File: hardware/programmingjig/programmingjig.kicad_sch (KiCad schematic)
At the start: 15 parts, among them J1 SPGM, J11 PGMIO, J2 USB_C_Receptacle_USB2.0, J3 PGMVDD, J4 PGMO, J5 PGMVDD-POGO-5.5mm, U2 RS3236-3.3YUTDN4, U3 CH32V003JxMx

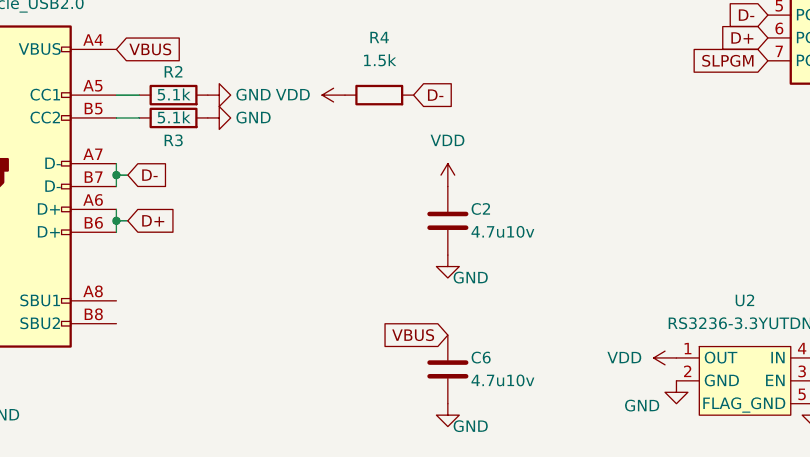
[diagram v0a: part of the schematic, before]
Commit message: Add firmware for programming jig
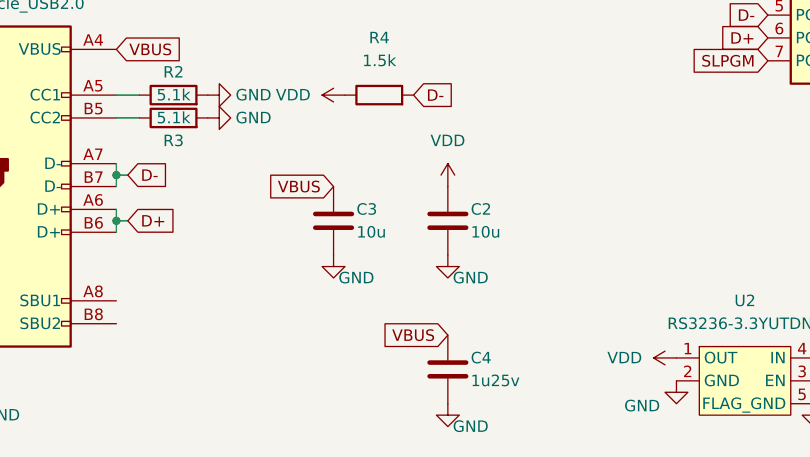
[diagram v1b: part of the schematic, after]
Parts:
- removed C6: 4.7u10v, Capacitor_SMD:C_0402_1005Metric, symbol Device:C
- added C3: 10u, Capacitor_SMD:C_0603_1608Metric, symbol Device:C
- added C4: 1u25v, Capacitor_SMD:C_0402_1005Metric, symbol Device:C
- C2: value 4.7u10v -> 10u; footprint Capacitor_SMD:C_0402_1005Metric -> Capacitor_SMD:C_0603_1608Metric; LCSC C23733 -> C19702
- J11, J3, J5: LCSC C5221281 -> C5221294
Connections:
- net GND: now also C3.2, C4.2
- net VBUS: now also C3.1, C4.1
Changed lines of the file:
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@@
+	(global_label "VBUS"
+		(shape input)
+		(at 101.6 60.96 180)
+		(fields_autoplaced yes)
+		(effects
+			(font
+				(size 1.27 1.27)
+			)
+			(justify right)
+		)
+		(property "Intersheetrefs" "${INTERSHEET_REFS}"
+			(at 94.2883 61.0394 0)
+			(effects
+				(font
+					(size 1.27 1.27)
+				)
+				(justify right)
+				(hide yes)
+			)
+		)
+	)
 	(global_label "VBUS"
 		(shape input)
@@
 			)
 		)
-		(property "LCSC" "C5221281"
+		(property "LCSC" "C5221294"
 			(at 218.44 60.96 0)
 			(effects
@@
 				(path "/fb00fef0-158e-4651-97d6-849960de9d61"
 					(reference "#PWR18")
+					(unit 1)
+				)
+			)
+		)
+	)
+	(symbol
+		(lib_id "power:GND")
+		(at 101.6 68.58 0)
+		(unit 1)
+		(exclude_from_sim no)
+		(in_bom yes)
+		(on_board yes)
+		(dnp no)
+		(property "Reference" "#PWR22"
+			(at 101.6 74.93 0)
+			(effects
+				(font
+					(size 1.27 1.27)
+				)
+				(hide yes)
+			)
+		)
+		(property "Value" "GND"
+			(at 104.14 71.12 0)
+			(effects
+				(font
+					(size 1.27 1.27)
+				)
+			)
+		)
+		(property "Footprint" ""
+			(at 101.6 68.58 0)
+			(effects
+				(font
+					(size 1.27 1.27)
+				)
+				(hide yes)
+			)
+		)
+		(property "Datasheet" ""
+			(at 101.6 68.58 0)
+			(effects
+				(font
+					(size 1.27 1.27)
+				)
+				(hide yes)
+			)
+		)
+		(property "Description" ""
+			(at 101.6 68.58 0)
+			(effects
+				(font
+					(size 1.27 1.27)
+				)
+				(hide yes)
+			)
+		)
+		(pin "1"
+		)
+		(instances
+			(project "programmingjig"
+				(path "/fb00fef0-158e-4651-97d6-849960de9d61"
+					(reference "#PWR22")
 					(unit 1)
 				)
@@
 	)
 	(symbol
+		(lib_id "Device:C")
+		(at 101.6 64.77 0)
+		(unit 1)
+		(exclude_from_sim no)
+		(in_bom yes)
+		(on_board yes)
+		(dnp no)
+		(property "Reference" "C3"
+			(at 104.14 63.5 0)
+			(effects
+				(font
+					(size 1.27 1.27)
+				)
+				(justify left)
+			)
+		)
+		(property "Value" "10u"
+			(at 104.14 66.04 0)
+			(effects
+				(font
+					(size 1.27 1.27)
+				)
+				(justify left)
+			)
+		)
+		(property "Footprint" "Capacitor_SMD:C_0603_1608Metric"
+			(at 102.5652 68.58 0)
+			(effects
+				(font
+					(size 1.27 1.27)
+				)
+				(hide yes)
+			)
+		)
+		(property "Datasheet" ""
+			(at 101.6 64.77 0)
+			(effects
+				(font
+					(size 1.27 1.27)
+				)
+				(hide yes)
+			)
+		)
+		(property "Description" ""
+			(at 101.6 64.77 0)
+			(effects
+				(font
+					(size 1.27 1.27)
+				)
+				(hide yes)
+			)
+		)
+		(property "LCSC" "C19702"
+			(at 101.6 64.77 0)
+			(effects
+				(font
+					(size 1.27 1.27)
+				)
+				(hide yes)
+			)
+		)
+		(pin "1"
+		)
+		(pin "2"
+		)
+		(instances
+			(project "programmingjig"
+				(path "/fb00fef0-158e-4651-97d6-849960de9d61"
+					(reference "C3")
+					(unit 1)
+				)
+			)
+		)
+	)
+	(symbol
 		(lib_id "Device:R")
 		(at 83.82 50.8 90)
@@
 			)
 		)
-		(property "LCSC" "C5221281"
+		(property "LCSC" "C5221294"
 			(at 218.44 68.58 0)
 			(effects
@@
 				(path "/fb00fef0-158e-4651-97d6-849960de9d61"
 					(reference "C1")
-					(unit 1)
-				)
-			)
-		)
-	)
-	(symbol
-		(lib_id "Device:C")
-		(at 114.3 81.28 0)
-		(unit 1)
-		(exclude_from_sim no)
-		(in_bom yes)
-		(on_board yes)
-		(dnp no)
-		(property "Reference" "C6"
-			(at 116.84 80.01 0)
-			(effects
-				(font
-					(size 1.27 1.27)
-				)
-				(justify left)
-			)
-		)
-		(property "Value" "4.7u10v"
-			(at 116.84 82.55 0)
-			(effects
-				(font
-					(size 1.27 1.27)
-				)
-				(justify left)
-			)
-		)
-		(property "Footprint" "Capacitor_SMD:C_0402_1005Metric"
-			(at 115.2652 85.09 0)
-			(effects
-				(font
-					(size 1.27 1.27)
-				)
-				(hide yes)
-			)
-		)
-		(property "Datasheet" ""
-			(at 114.3 81.28 0)
-			(effects
-				(font
-					(size 1.27 1.27)
-				)
-				(hide yes)
-			)
-		)
-		(property "Description" ""
-			(at 114.3 81.28 0)
-			(effects
-				(font
-					(size 1.27 1.27)
-				)
-				(hide yes)
-			)
-		)
-		(property "LCSC" "C23733"
-			(at 114.3 81.28 0)
-			(effects
-				(font
-					(size 1.27 1.27)
-				)
-				(hide yes)
-			)
-		)
-		(pin "1"
-		)
-		(pin "2"
-		)
-		(instances
-			(project "programmingjig"
-				(path "/fb00fef0-158e-4651-97d6-849960de9d61"
-					(reference "C6")
 					(unit 1)
 				)
@@
 			)
 		)
-		(property "LCSC" "C5221281"
+		(property "LCSC" "C5221294"
 			(at 218.44 53.34 0)
 			(effects
@@
 				(path "/fb00fef0-158e-4651-97d6-849960de9d61"
 					(reference "J11")
+					(unit 1)
+				)
+			)
+		)
+	)
+	(symbol
+		(lib_id "Device:C")
+		(at 114.3 81.28 0)
+		(unit 1)
+		(exclude_from_sim no)
+		(in_bom yes)
+		(on_board yes)
+		(dnp no)
+		(property "Reference" "C4"
+			(at 116.84 80.01 0)
+			(effects
+				(font
+					(size 1.27 1.27)
+				)
+				(justify left)
+			)
+		)
+		(property "Value" "1u25v"
+			(at 116.84 82.55 0)
+			(effects
+				(font
+					(size 1.27 1.27)
+				)
+				(justify left)
+			)
+		)
+		(property "Footprint" "Capacitor_SMD:C_0402_1005Metric"
+			(at 115.2652 85.09 0)
+			(effects
+				(font
+					(size 1.27 1.27)
+				)
+				(hide yes)
+			)
+		)
+		(property "Datasheet" ""
+			(at 114.3 81.28 0)
+			(effects
+				(font
+					(size 1.27 1.27)
+				)
+				(hide yes)
+			)
+		)
+		(property "Description" ""
+			(at 114.3 81.28 0)
+			(effects
+				(font
+					(size 1.27 1.27)
+				)
+				(hide yes)
+			)
+		)
+		(property "LCSC" "C52923"
+			(at 114.3 81.28 0)
+			(effects
+				(font
+					(size 1.27 1.27)
+				)
+				(hide yes)
+			)
+		)
+		(pin "1"
+		)
+		(pin "2"
+		)
+		(instances
+			(project "programmingjig"
+				(path "/fb00fef0-158e-4651-97d6-849960de9d61"
+					(reference "C4")
 					(unit 1)
 				)
@@
 			)
 		)
-		(property "Value" "4.7u10v"
+		(property "Value" "10u"
 			(at 116.84 66.04 0)
 			(effects
@@
 			)
 		)
-		(property "Footprint" "Capacitor_SMD:C_0402_1005Metric"
+		(property "Footprint" "Capacitor_SMD:C_0603_1608Metric"
 			(at 115.2652 68.58 0)
 			(effects
@@
 			)
 		)
-		(property "LCSC" "C23733"
+		(property "LCSC" "C19702"
 			(at 114.3 64.77 0)
 			(effects
@@
 		(on_board yes)
 		(dnp no)
-		(fields_autoplaced yes)
 		(property "Reference" "U3"
 			(at 169.7833 34.29 0)
